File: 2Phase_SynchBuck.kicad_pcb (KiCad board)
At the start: 4 copper layers, 100 x 67 mm, 308 parts, among them CN201 04A2, CN202 04A2, CN203 04A2, CN204 04A2, CN205 SMA-J-P-H-ST-EM1, CN701 USB4215-03-A, CN702 Conn_JTAG_STDC10, CN703 FFC2B28-16-G, CN704 FFC2B28-04-G, Q101 BSZ018N04LS6, Q102 IQE013N04LM6, Q103 BSZ018N04LS6, Q104 IQE013N04LM6, Q105 GS2N7002KW, Q106 GS2N7002KW, Q801 GS2N7002KW, Q802 GS2N7002KW, Q803 GS2N7002KW, Q804 GS2N7002KW, SW901 SW_SPDT, U101 UCC27282DRC, U102 ACS37030LLZATR-040B3, U103 UCC27282DRC, U104 ACS37030LLZATR-040B3, U106 INA187A1IDBVR, U301 LMR54410DBVR, U302 LMR54410DBVR, U303 SPX3819M5-L-3-3/TR, U304 SPX3819M5-L-3-3/TR, U305 LDLN025M33R, U306 LM66100DCK, U401 STM32G474RET6, U402 MCP1501T-30E, U601 TLV9061SIDBVR, U602 TLV9061SIDBVR, U701 USBLC6-2SC6, X501 ABM11W-24MHz-8

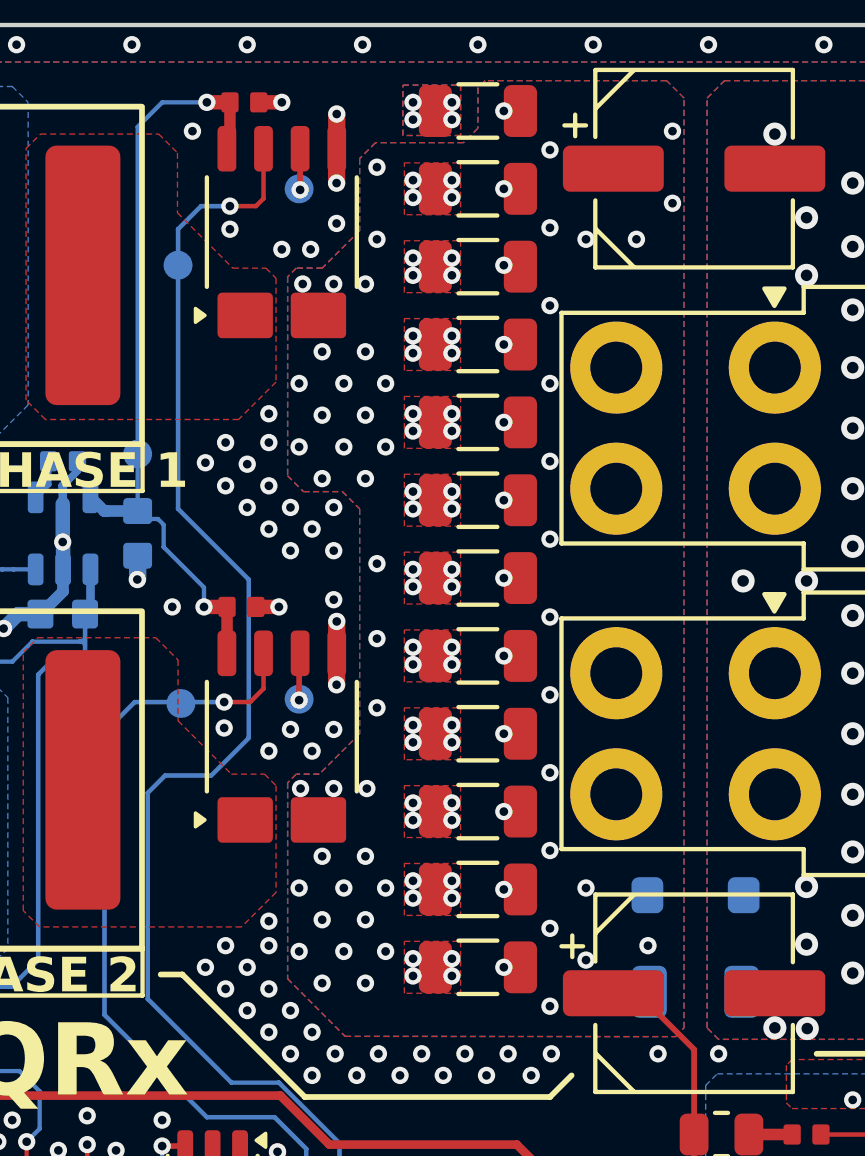
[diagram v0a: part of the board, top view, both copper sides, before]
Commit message: Update 2Phase_SynchBuck.kicad_pcb
Restored outer via annular ring
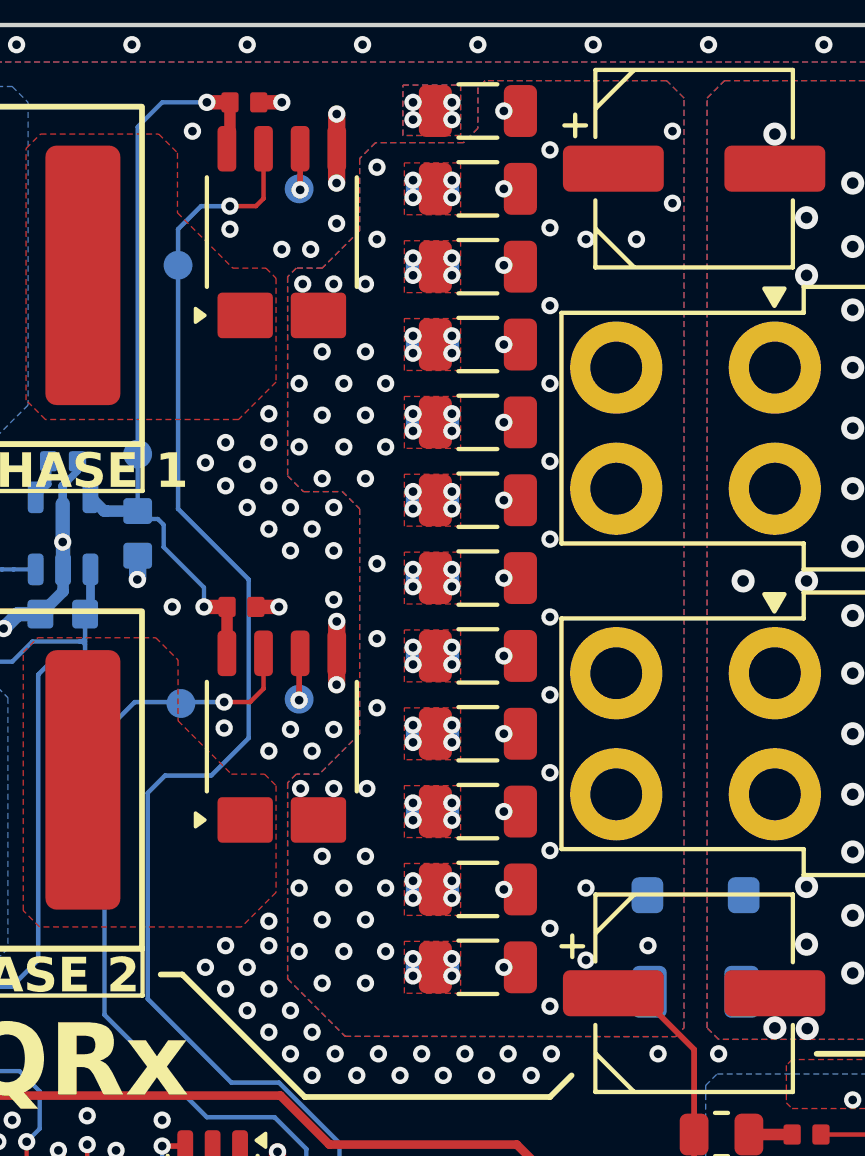
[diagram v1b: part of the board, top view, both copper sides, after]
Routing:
- net GND: track 156.9 -> 170.1 mm
